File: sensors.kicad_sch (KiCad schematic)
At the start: 41 parts, among them Q801 IRLML6402, Q802 IRLML6402, Q803 IRLML6402, Q804 IRLML6402, Q805 IRLML6402, U801 TPS61023DRLR, U802 ISL83078EIBZA

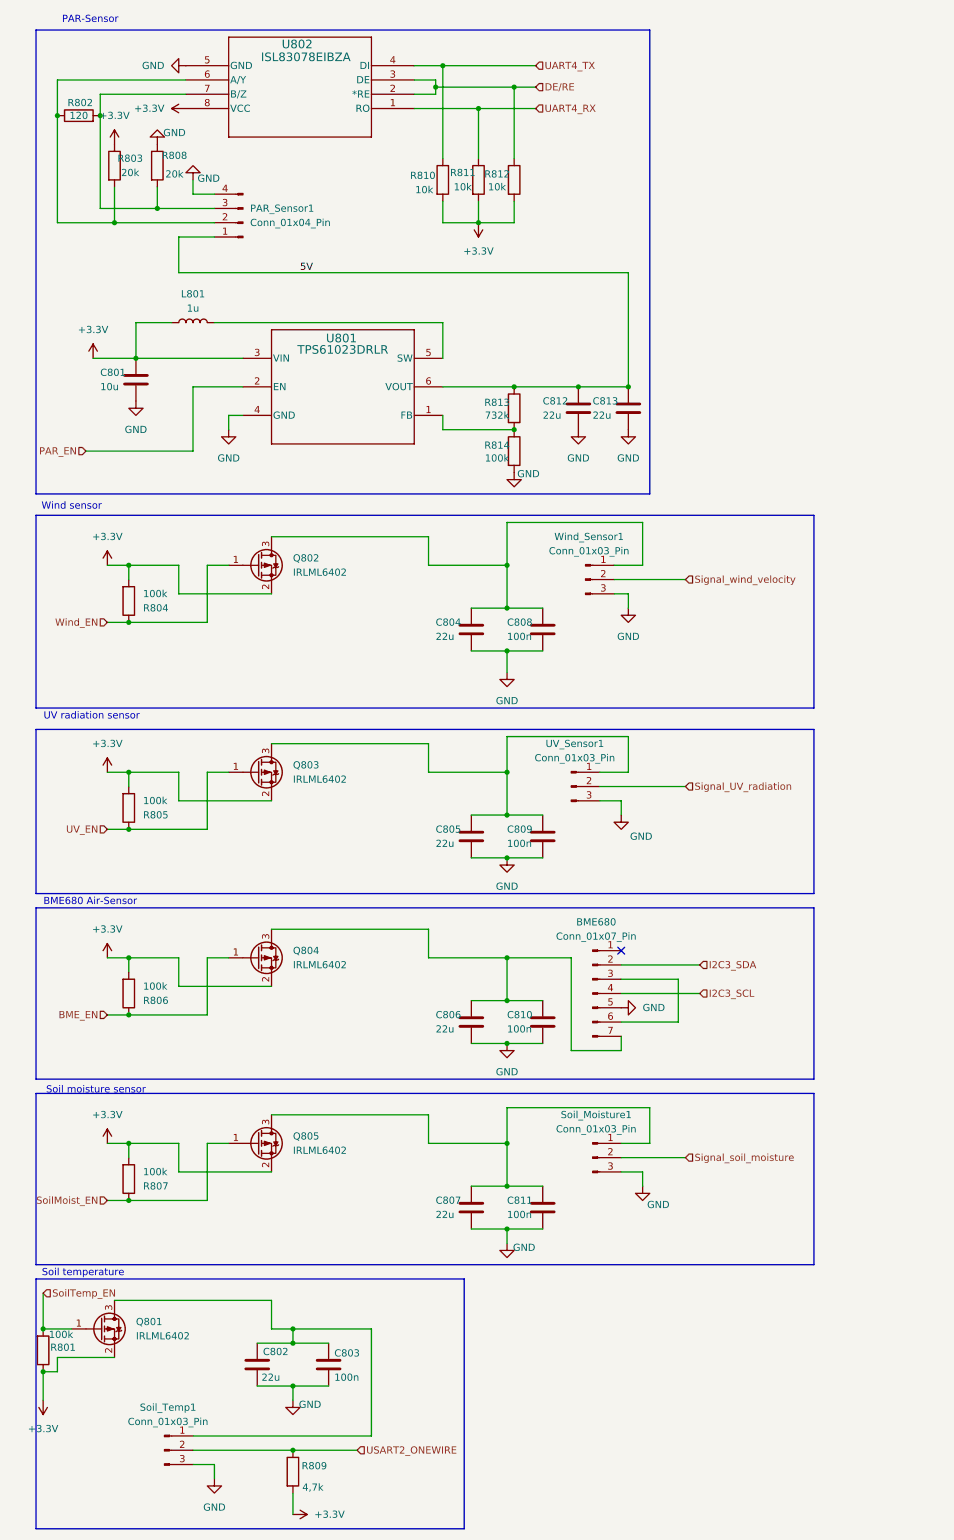
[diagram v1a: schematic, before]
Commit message: new layout
- recreation of the layout
- changed connection of ADC to MCU
- cleaner layout
- battery (supercap) for rtc
- crystal nearby the mcu
- 3V3 layer can be switched on/off separated from the mcu
- diode replaced with MOSFET
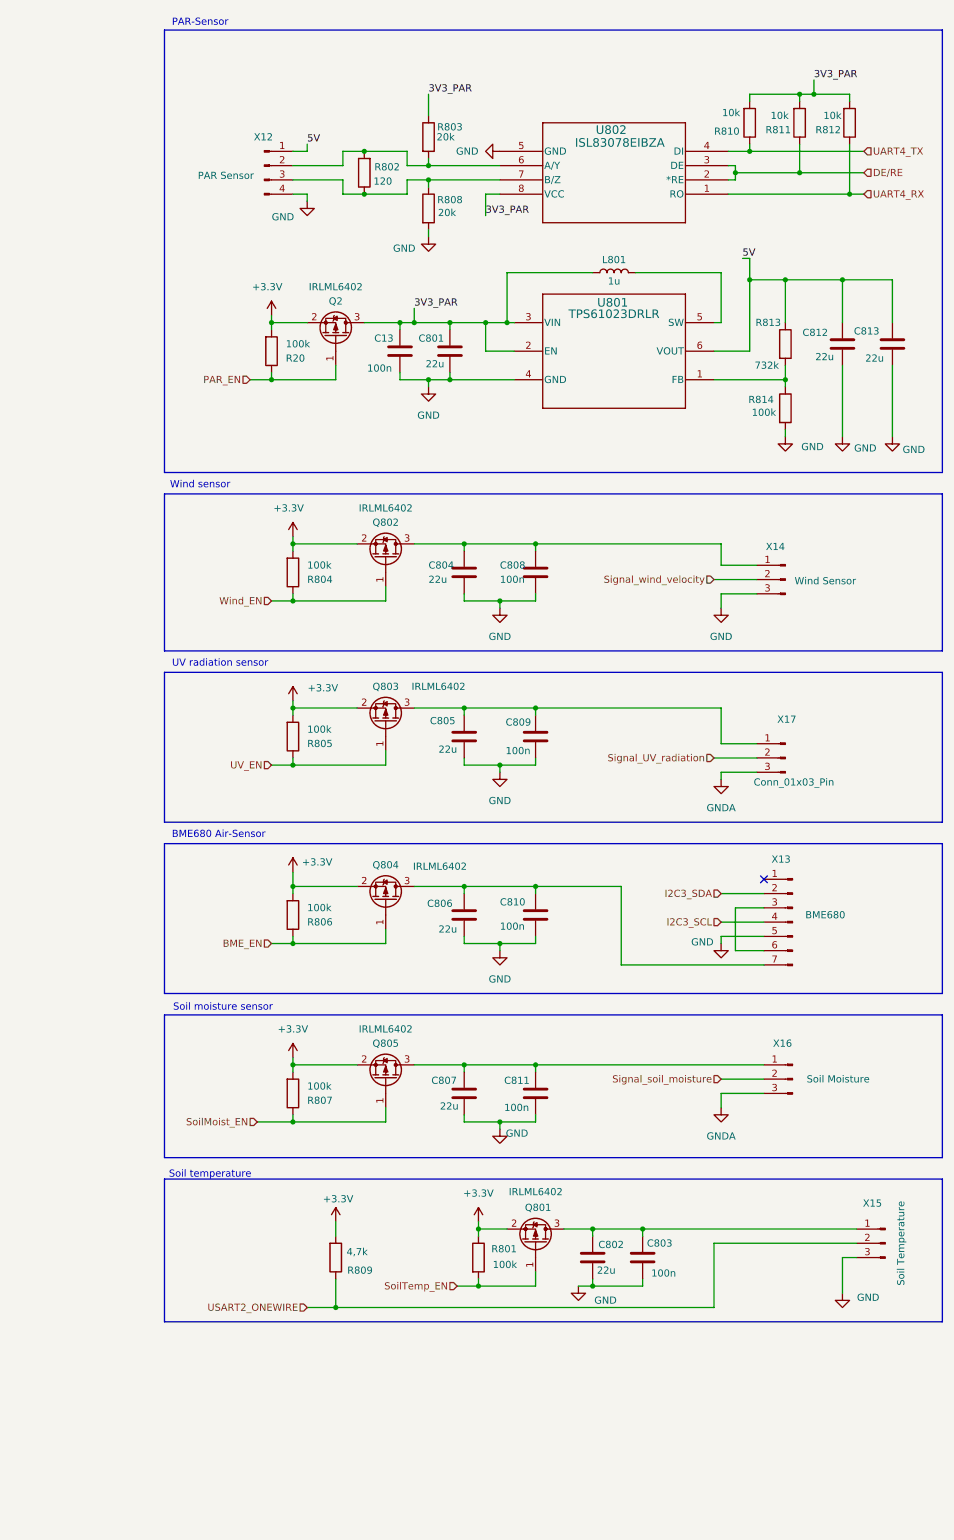
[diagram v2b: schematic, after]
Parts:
- added C13: 100n, Capacitor_SMD:C_0805_2012Metric_Pad1.18x1.45mm_HandSolder, symbol Device:C
- added Q2: IRLML6402, Package_TO_SOT_SMD:SOT-23, symbol Transistor_FET:IRLML6402
- added R20: 100k, Resistor_SMD:R_0805_2012Metric_Pad1.20x1.40mm_HandSolder, symbol Device:R
- C801: value 10u -> 22u
- C803, C808, C809, C810, C811: Mouser Part Number 187-CL21A226KQCLRNC -> 603-CC805KRX7R9BB104
- L801: Mouser Part Number (none) -> 80-C0805C105K3RACTM
- Q801, Q802, Q803, Q804, Q805: Mouser Part Number (none) -> 942-IRLML6402TRPBF
- R802: Mouser Part Number 279-CRG0805ZR -> 652-CR0805JW-121ELF
- R803, R808: Mouser Part Number 279-CRG0805ZR -> 660-RK73B2ATTD203J
- R809: Mouser Part Number 279-CRG0805ZR -> 279-CRG0805F4K7
- R810, R811, R812: Mouser Part Number 279-CRG0805ZR -> 660-RK73B2ATTD103G
- R813: Mouser Part Number 279-CRG0805ZR -> 603-RT0805FRE07732KL
- R814: Mouser Part Number 279-CRG0805ZR -> 660-RK73B2ATTE104J
- U801: Mouser Part Number (none) -> 595-TPS61023DRLR
- U802: Mouser Part Number (none) -> 968-ISL83078EIBZA
- X12: renamed from PAR_Sensor1; Mouser Part Number (none) -> 306-B4BXHAMLFSNP
- X13: renamed from BME680; Mouser Part Number (none) -> 306-B7BXHAMLFSNP
- X14: renamed from Wind_Sensor1; Mouser Part Number (none) -> 306-B3BXHAMLFSNP
- X15: renamed from Soil_Temp1; Mouser Part Number (none) -> 306-B3BXHAMLFSNP
- X16: renamed from Soil_Moisture1; Mouser Part Number (none) -> 306-B3BXHAMLFSNP
- X17: renamed from UV_Sensor1; Mouser Part Number (none) -> 306-B3BXHAMLFSNP
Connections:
- net +3.3V: now also Q2.2 (S), R20.2; no longer C801.2, L801.1, R803.1, R810.2, R811.2, R812.2, U801.3 (VIN), U802.8 (VCC)
- net DE/RE: now also R811.1; no longer R812.1
- net GND: now also R808.2, C13.1; no longer R808.1, X16.3 (Pin_3), X17.3 (Pin_3)
- net PAR_EN: now also Q2.1 (G), R20.1; no longer U801.2 (EN)
- net UART4_RX: now also R812.1; no longer R811.1
- net at R803.2, U802.6 (A/Y), X12.2 (Pin_2): now also R802.2; no longer R802.1
- net at U802.7 (B/Z), X12.3 (Pin_3): now also R802.1, R808.1; no longer R802.2, R808.2
- new net 3V3_PAR: C13.2, C801.2, L801.1, Q2.3 (D), R803.1, R810.2, R811.2, R812.2, U801.2 (EN), U801.3 (VIN), U802.8 (VCC)
- new net GNDA: X16.3 (Pin_3), X17.3 (Pin_3)
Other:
- moved on the sheet: C801, C802, C803, C804, C805, C806, C807, C808, C809, C810, C811, C812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
